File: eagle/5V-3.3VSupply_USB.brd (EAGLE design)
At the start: 45.4 x 71.1 mm, 27 parts, among them IC1 NJM2396, IC2 TA48M033F, IC3 LM358N, J1 DCIN, J2 5VOUT, J3 3V3OUT

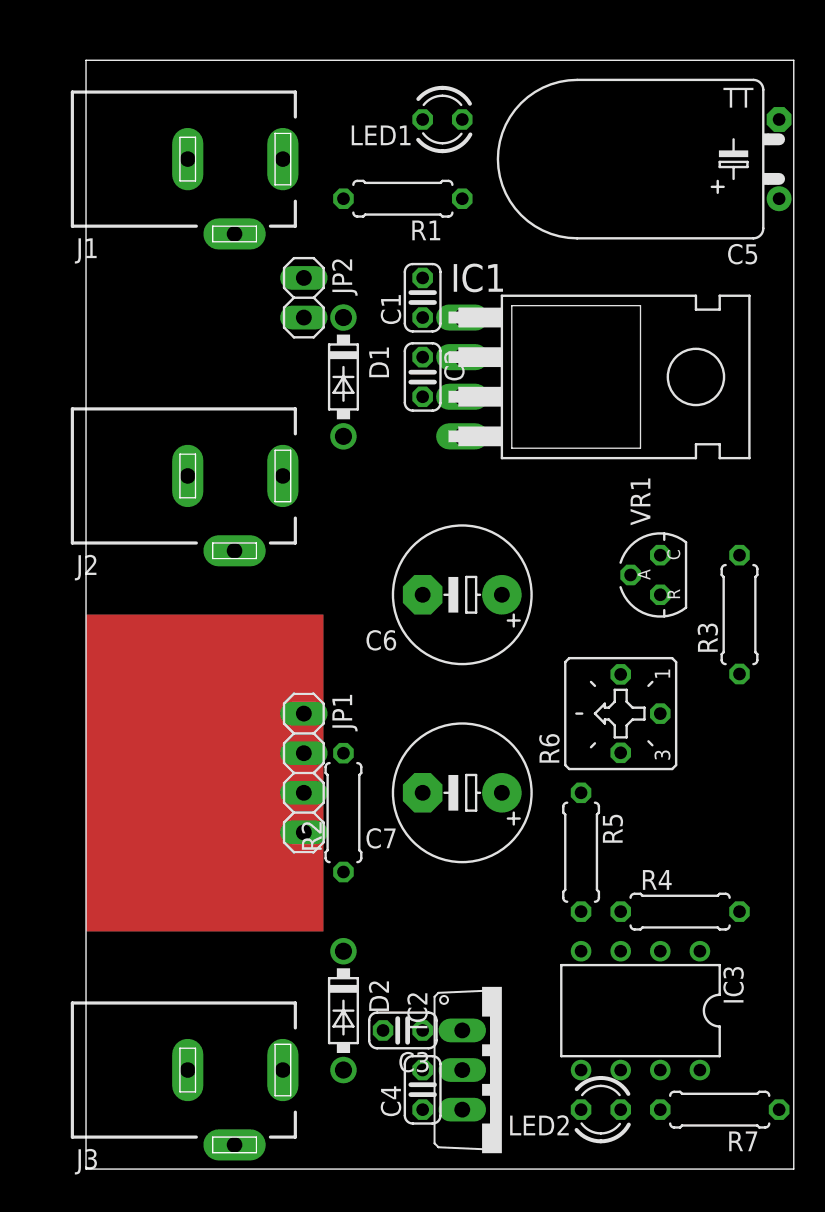
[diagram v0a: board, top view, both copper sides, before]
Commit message: 基板図配置修正
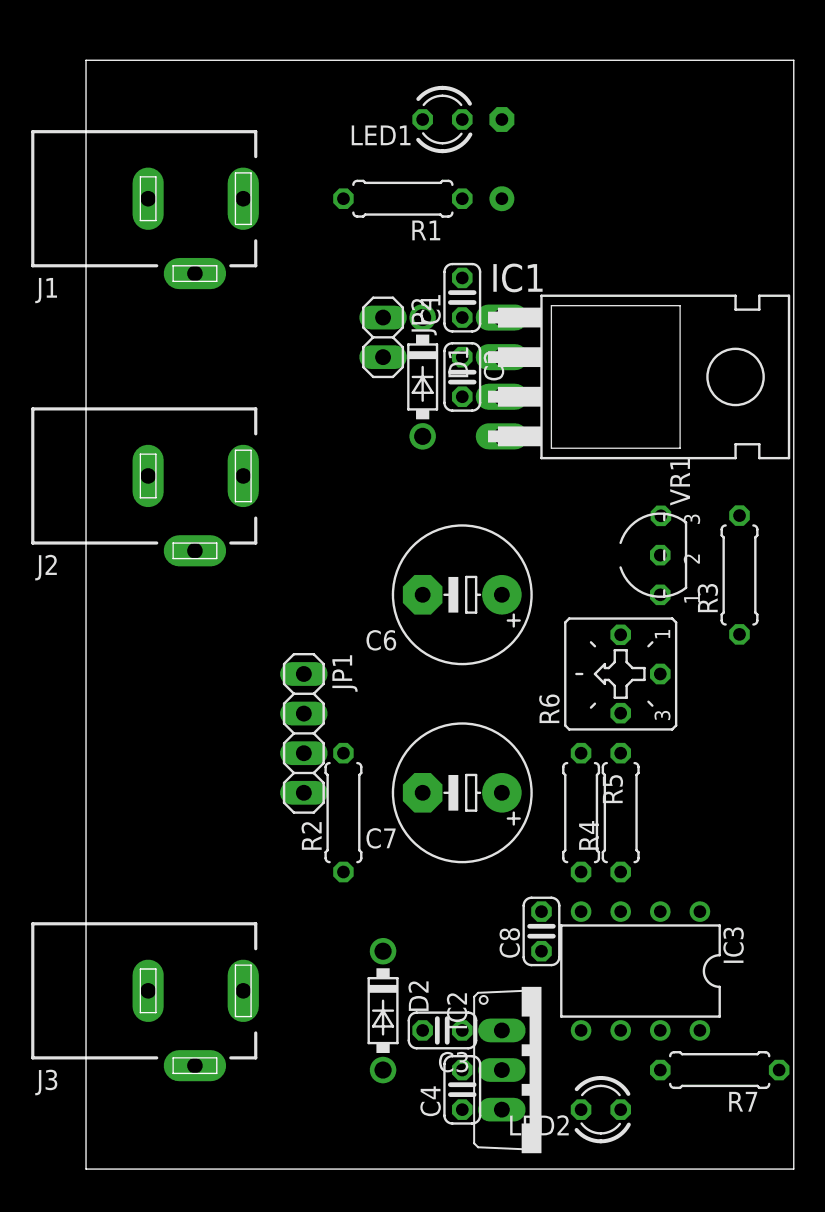
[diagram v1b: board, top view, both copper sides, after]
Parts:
- added C8: 0.1uF, rcl:C025-024X044
- LED1: value BLUE -> GREEN
- VR1: device v-reg:TO92-CLP -> mylib2:TO226AA
- moved C5 17.8 mm to (27.9, 66.0), flipped to the bottom
- moved R4 7.41 mm to (35.6, 24.1), turned to 90 degrees
- moved J3 5.68 mm to (8.26, 12.7)
- moved JP2 5.68 mm to (20.3, 54.6)
- moved D1 5.08 mm to (22.9, 52.1)
- moved J1 3.59 mm to (8.26, 63.5)
- moved R6 2.54 mm to (35.6, 33.0)
- moved IC3 2.54 mm to (36.8, 14.0)
- moved R7 2.54 mm to (41.9, 7.62)
- moved C1 2.54 mm to (25.4, 57.1)
- moved C2 2.54 mm to (25.4, 52.1)
- moved C3 2.54 mm to (24.1, 10.2)
- moved C4 2.54 mm to (25.4, 6.35)
- moved D2 2.54 mm to (20.3, 11.4)
- moved IC1 2.54 mm to (40.6, 52.1)
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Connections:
- net GND: now also C8.2, VR1.2; no longer VR1.A
- net N$1: now also C8.1
- net N$8: now also VR1.1, VR1.3; no longer VR1.C, VR1.R

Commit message: 基板図修正
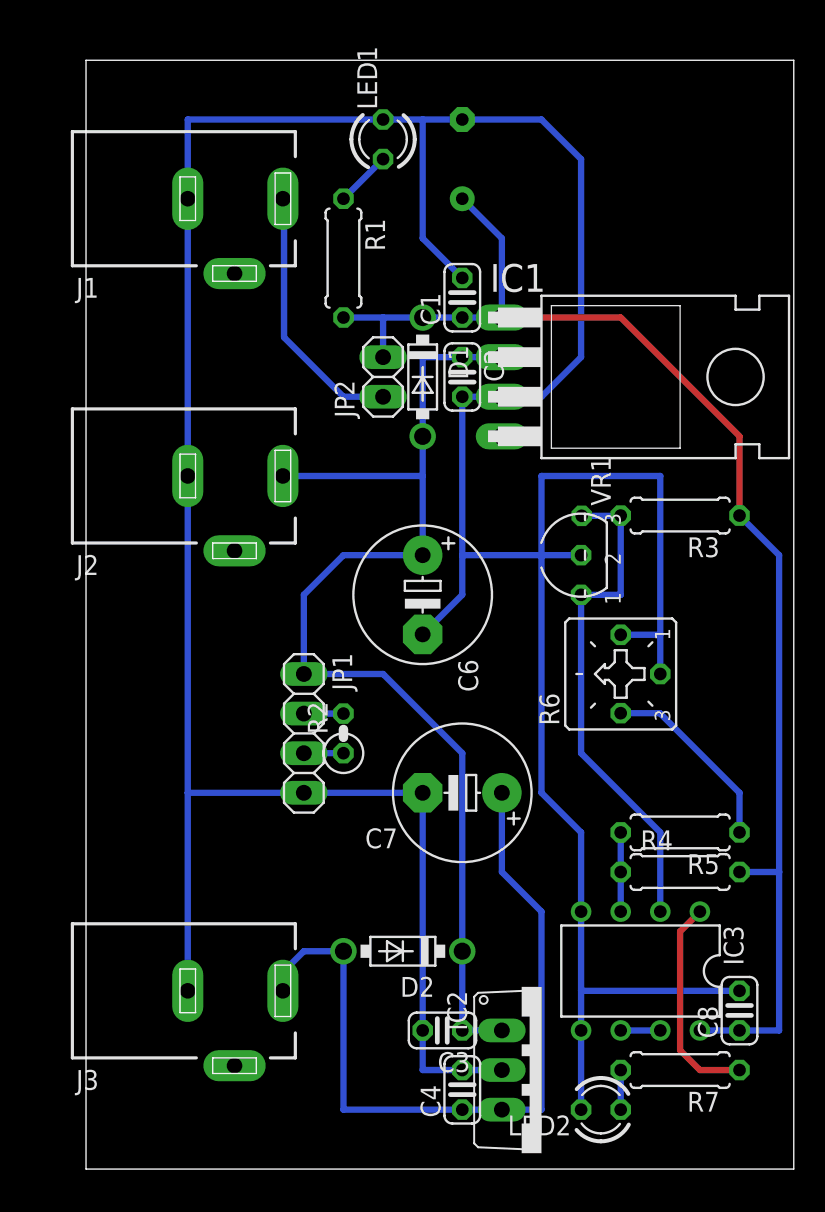
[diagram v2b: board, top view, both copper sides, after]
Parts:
- R2: device rcl:0207/7 -> rcl:0207/2V
- moved C8 13.7 mm to (43.2, 11.4)
- moved R5 6.48 mm to (39.4, 22.9), turned to 180 degrees
- moved R3 5.39 mm to (39.4, 43.2), turned to 180 degrees
- moved R1 5.39 mm to (17.8, 59.7), turned to 270 degrees
- moved R4 5.39 mm to (39.4, 20.3), turned to 0 degrees
- moved R2 5.08 mm to (17.8, 29.2)
- moved VR1 5.08 mm to (33.0, 40.6)
- moved D2 4.02 mm to (21.6, 15.2), turned to 180 degrees
- moved LED1 4.02 mm to (20.3, 67.3), turned to 90 degrees
- moved C5 2.54 mm to (25.4, 66.0)
- moved C6 2.54 mm to (22.9, 38.1), turned to 270 degrees
- moved J1 2.54 mm to (10.8, 63.5)
- moved J2 2.54 mm to (10.8, 45.7)
- moved J3 2.54 mm to (10.8, 12.7)
- moved JP2 2.54 mm to (20.3, 52.1), turned to 90 degrees
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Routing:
- net GND: track 0.00 -> 251.3 mm
- net N$1: track 0.00 -> 86.5 mm
- net N$2: track 0.00 -> 73.1 mm
- net N$3: track 0.00 -> 49.9 mm
- net N$8: track 0.00 -> 32.5 mm
- net N$5: track 0.00 -> 16.8 mm
- net N$11: track 0.00 -> 13.8 mm
- net N$10: track 0.00 -> 12.3 mm
- net N$9: track 0.00 -> 5.08 mm
- net N$4: track 0.00 -> 3.59 mm
- net N$7: track 0.00 -> 2.54 mm
- net N$6: track 0.00 -> 2.54 mm
- net N$12: track 0.00 -> 2.54 mm
- net N$13: track 0.00 -> 2.54 mm

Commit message: コンパレーターの入力の正負を入れ替え
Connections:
- net N$8: now also IC3.3; no longer IC3.2
- net N$9: now also IC3.2; no longer IC3.3
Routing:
- net N$9: track 5.08 -> 7.62 mm
- net N$8: track 32.5 -> 31.5 mm
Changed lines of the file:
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@@
 <contactref element="R4" pad="1"/>
 <contactref element="R5" pad="2"/>
-<contactref element="IC3" pad="3"/>
-<wire x1="35.56" y1="17.78" x2="35.56" y2="20.32" width="0.4064" layer="16"/>
 <wire x1="35.56" y1="22.86" x2="35.56" y2="20.32" width="0.4064" layer="16"/>
+<contactref element="IC3" pad="2"/>
+<wire x1="35.56" y1="20.32" x2="38.1" y2="20.32" width="0.4064" layer="16"/>
+<wire x1="38.1" y1="20.32" x2="38.1" y2="17.78" width="0.4064" layer="16"/>
 </signal>
 <signal name="N$10">
@@
 <signal name="N$8">
 <contactref element="R3" pad="2"/>
-<contactref element="IC3" pad="2"/>
 <contactref element="VR1" pad="3"/>
 <contactref element="VR1" pad="1"/>
-<wire x1="33.02" y1="27.94" x2="33.02" y2="38.095475" width="0.4064" layer="16"/>
-<wire x1="33.02" y1="38.095475" x2="33.020340625" y2="38.095815625" width="0.4064" layer="16"/>
 <wire x1="33.059709375" y1="43.16389375" x2="35.54389375" y2="43.16389375" width="0.4064" layer="16"/>
 <wire x1="35.54389375" y1="43.16389375" x2="35.56" y2="43.18" width="0.4064" layer="16"/>
+<contactref element="IC3" pad="3"/>
+<wire x1="35.56" y1="17.78" x2="34.29" y2="19.05" width="0.4064" layer="1"/>
+<wire x1="34.29" y1="19.05" x2="34.29" y2="24.13" width="0.4064" layer="1"/>
+<wire x1="34.29" y1="24.13" x2="33.02" y2="25.4" width="0.4064" layer="1"/>
+<wire x1="33.02" y1="25.4" x2="33.02" y2="38.095475" width="0.4064" layer="1"/>
+<wire x1="33.02" y1="38.095475" x2="33.020340625" y2="38.095815625" width="0.4064" layer="1"/>
 <wire x1="33.020340625" y1="38.095815625" x2="35.555815625" y2="38.095815625" width="0.4064" layer="16"/>
 <wire x1="35.555815625" y1="38.095815625" x2="35.56" y2="38.1" width="0.4064" layer="16"/>
 <wire x1="35.56" y1="38.1" x2="35.56" y2="43.18" width="0.4064" layer="16"/>
-<wire x1="38.1" y1="17.78" x2="38.1" y2="22.86" width="0.4064" layer="16"/>
-<wire x1="38.1" y1="22.86" x2="33.02" y2="27.94" width="0.4064" layer="16"/>
 </signal>
 </signals>
